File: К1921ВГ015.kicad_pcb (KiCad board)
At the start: 2 copper layers, 100 x 100 mm, 102 parts, among them J1 SERVEN, J11 Conn_02x05_Odd_Even, J12 AREF-TEST/MODULE, J14 Power DC 5V, J2 JTAG, J3 SELECT, J4 5V, J5 PORT-A-0-15, J6 Conn_02x22_Odd_Even, J7 Conn_02x22_Odd_Even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

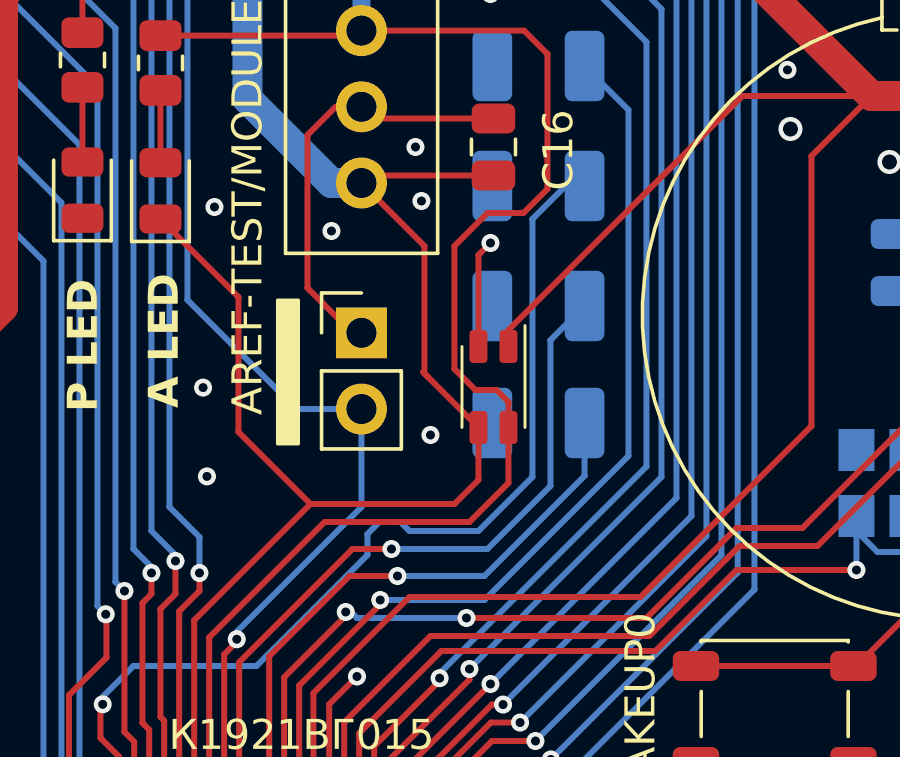
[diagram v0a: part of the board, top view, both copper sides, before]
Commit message: Add AGND capacitors
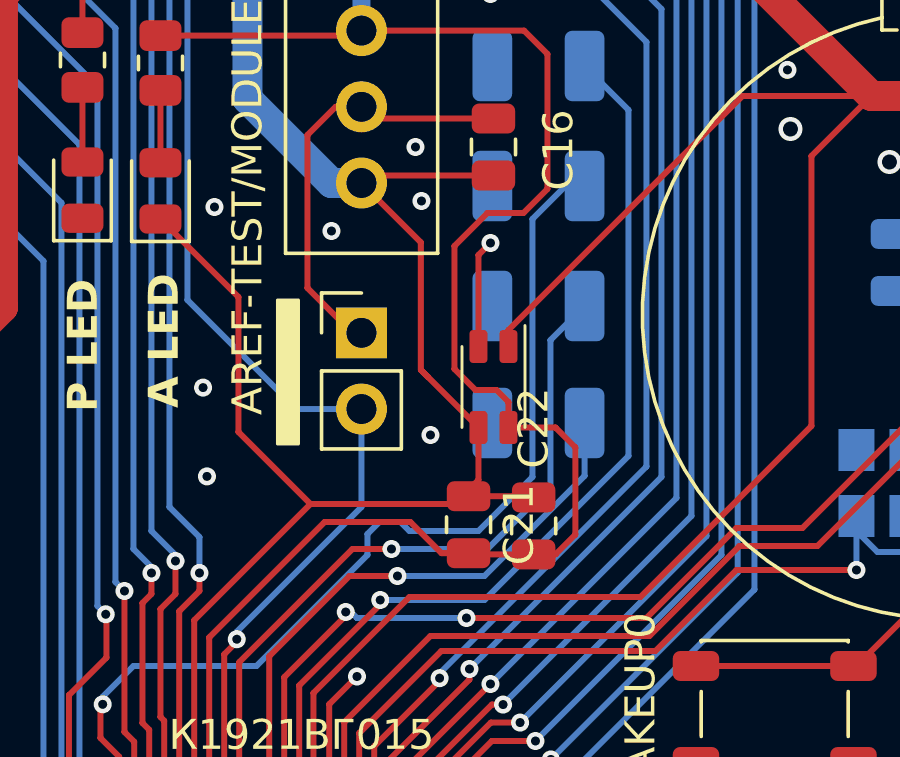
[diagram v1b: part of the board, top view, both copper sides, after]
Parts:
- added C21: 10nF, Capacitor_SMD:C_0805_2012Metric, F.Cu at (158.3, 67.3)
- added C22: 100nF, Capacitor_SMD:C_0805_2012Metric, F.Cu at (160.4, 67.3)
- RV1: value 10k -> 1k
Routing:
- net AVCC: track 60.6 -> 66.6 mm
- net AGND: track 172.5 -> 174.6 mm

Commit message: Update APower
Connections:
- C17 pad 2: GND1 -> AGND
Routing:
- net AGND: track 174.6 -> 179.0 mm
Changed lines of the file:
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@@
 			(layers "B.Cu" "B.Mask" "B.Paste")
 			(roundrect_rratio 0.188679)
-			(net 1 "GND1")
+			(net 37 "AGND")
 			(pintype "passive")
 		)
@@
 	)
 	(via
-		(at 156.7 56.5)
+		(at 156.829265 57.180735)
 		(size 0.6)
 		(drill 0.3)
@@
 	)
 	(segment
+		(start 159.0625 56)
+		(end 158.9625 55.9)
+		(width 0.2)
+		(layer "B.Cu")
+		(net 37)
+	)
+	(segment
 		(start 153.7 55.9)
 		(end 154.7 55.9)
@@
 	)
 	(segment
+		(start 158.9625 55.9)
+		(end 154.7 55.9)
+		(width 0.2)
+		(layer "B.Cu")
+		(net 37)
+	)
+	(segment
 		(start 161.251106 76)
 		(end 159.45 76)
@@
 	)
 	(segment
-		(start 160.4 65.7)
-		(end 160.4 57.1)
-		(width 0.2)
-		(layer "B.Cu")
-		(net 47)
-	)
-	(segment
-		(start 146.074714 73.025286)
-		(end 147.1 72)
+		(start 160.4 57.1)
+		(end 161.5 56)
 		(width 0.2)
 		(layer "B.Cu")
@@
 	)
 	(segment
-		(start 155.3 67.2)
-		(end 156 67.2)
+		(start 151.2 72)
+		(end 154.9 68.3)
 		(width 0.2)
 		(layer "B.Cu")
@@
 	)
 	(segment
-		(start 160.4 57.1)
-		(end 161.5 56)
+		(start 154.9 68.3)
+		(end 154.9 67.6)
 		(width 0.2)
 		(layer "B.Cu")
@@
 	)
 	(segment
-		(start 147.1 72)
-		(end 151.2 72)
+		(start 154.9 67.6)
+		(end 155.3 67.2)
 		(width 0.2)
 		(layer "B.Cu")
@@
 	)
 	(segment
-		(start 151.2 72)
-		(end 154.9 68.3)
+		(start 158.9 67.2)
+		(end 160.4 65.7)
 		(width 0.2)
 		(layer "B.Cu")
@@
 	)
 	(segment
-		(start 154.9 67.6)
-		(end 155.3 67.2)
+		(start 147.1 72)
+		(end 151.2 72)
 		(width 0.2)
 		(layer "B.Cu")
@@
 	)
 	(segment
-		(start 156 67.2)
-		(end 156.3 67.5)
+		(start 146.074714 73.025286)
+		(end 147.1 72)
 		(width 0.2)
 		(layer "B.Cu")
@@
 	)
 	(segment
-		(start 158.6 67.5)
-		(end 160.4 65.7)
-		(width 0.2)
-		(layer "B.Cu")
-		(net 47)
-	)
-	(segment
-		(start 161.5 56)
-		(end 162.1375 56)
+		(start 155.3 67.2)
+		(end 158.9 67.2)
 		(width 0.2)
 		(layer "B.Cu")
@@
 	)
 	(segment
-		(start 156.3 67.5)
-		(end 158.6 67.5)
+		(start 160.4 65.7)
+		(end 160.4 57.1)
 		(width 0.2)
 		(layer "B.Cu")
@@
 	)
 	(segment
-		(start 154.9 68.3)
-		(end 154.9 67.6)
+		(start 161.5 56)
+		(end 162.1375 56)
 		(width 0.2)
 		(layer "B.Cu")
